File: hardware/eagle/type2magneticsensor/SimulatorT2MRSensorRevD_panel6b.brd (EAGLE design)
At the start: 99.1 x 96.5 mm, 83 parts, among them U1A 2SS52MOFFSET, U1A_1 2SS52MOFFSET, U1A_2 2SS52MOFFSET, U1A_3 2SS52MOFFSET, U1A_4 2SS52MOFFSET, U1A_5 2SS52MOFFSET, U1B 2SS52MOFFSET, U1B_1 2SS52MOFFSET, U1B_2 2SS52MOFFSET, U1B_3 2SS52MOFFSET, U1B_4 2SS52MOFFSET, U1B_5 2SS52MOFFSET

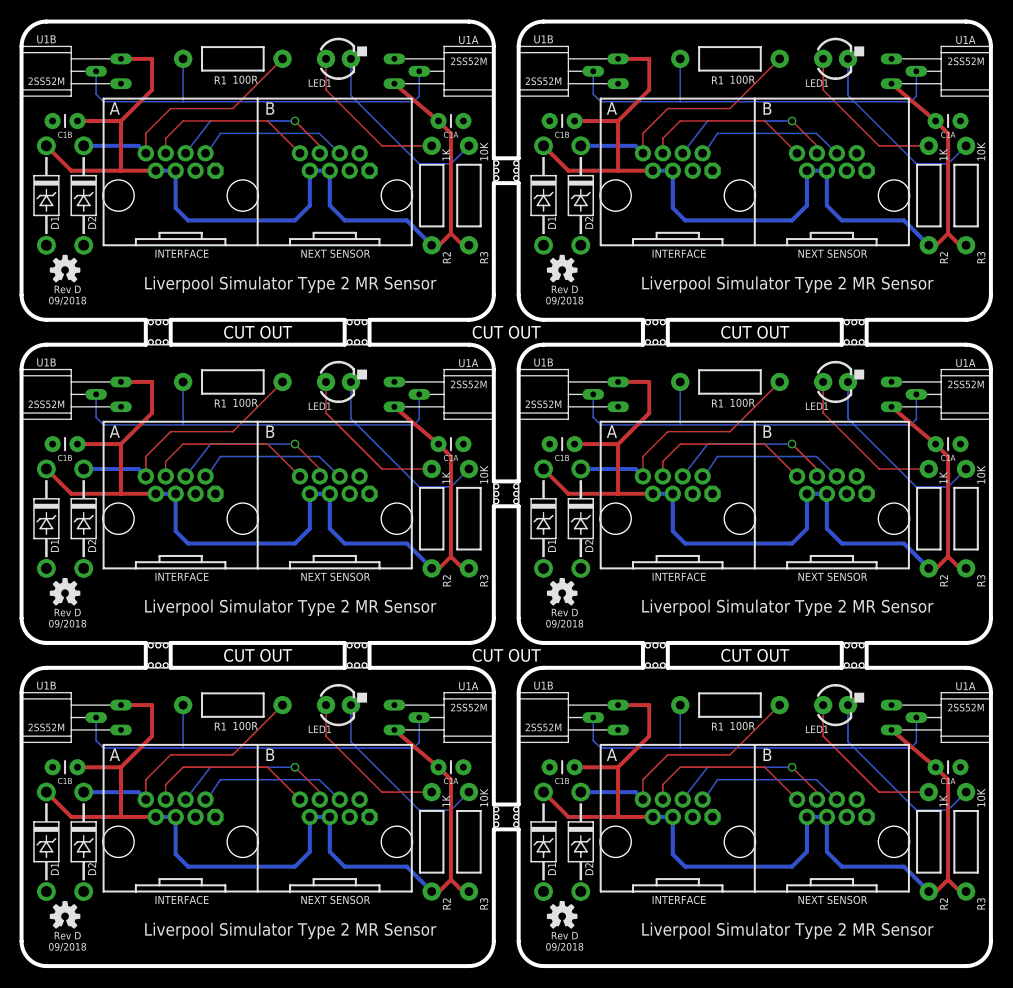
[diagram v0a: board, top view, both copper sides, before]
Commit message: Wider 5mm break-offs
Issues with JLPCB rejecting panelised boards with 2.5mm stamp hole
break-off tabs. Increased tab width to 5mm on all panelised boards.
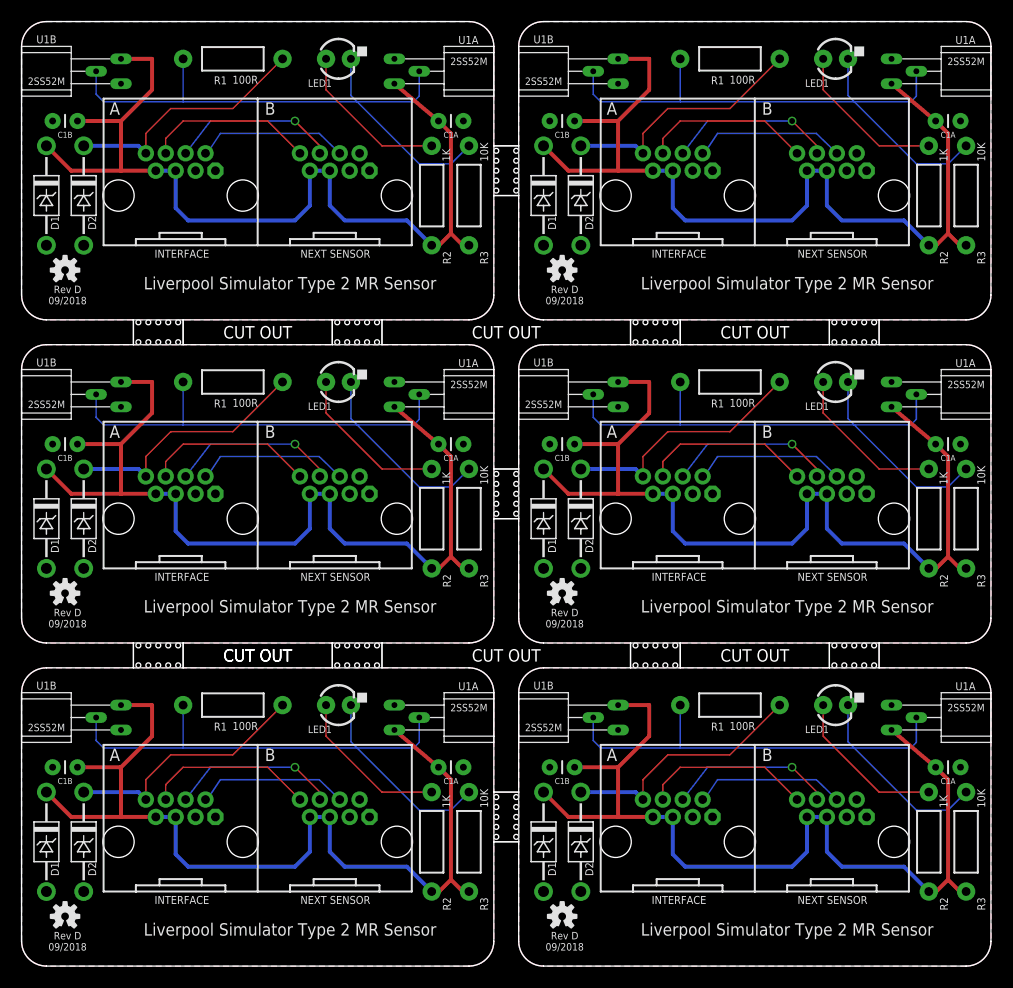
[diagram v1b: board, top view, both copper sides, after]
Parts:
- removed E$1, E$10, E$11, E$2, E$3, E$4, E$5, E$6, E$7, E$8, E$9: (no value), AIC_Custom:STAMP_HOLES
- added E$12: (no value), AIC_Custom:OUTLINE_PANEL_6_5MM
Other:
- outline, holes or cut-outs redrawn
